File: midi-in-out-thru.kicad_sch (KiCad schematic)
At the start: 24 parts, among them J1 uC, J2 IN, J3 OUT, J4 THRU, U1 74HC14, U2 H11L1

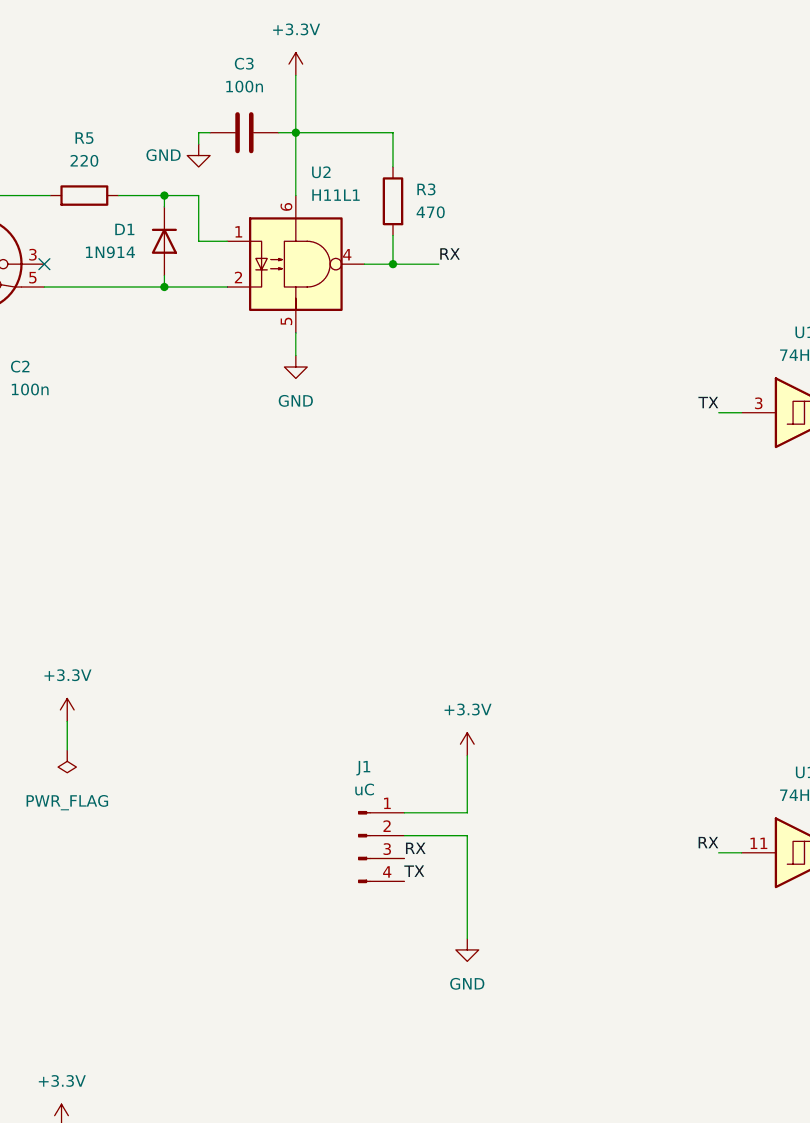
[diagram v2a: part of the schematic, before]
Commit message: Smaller resistors, neater layout
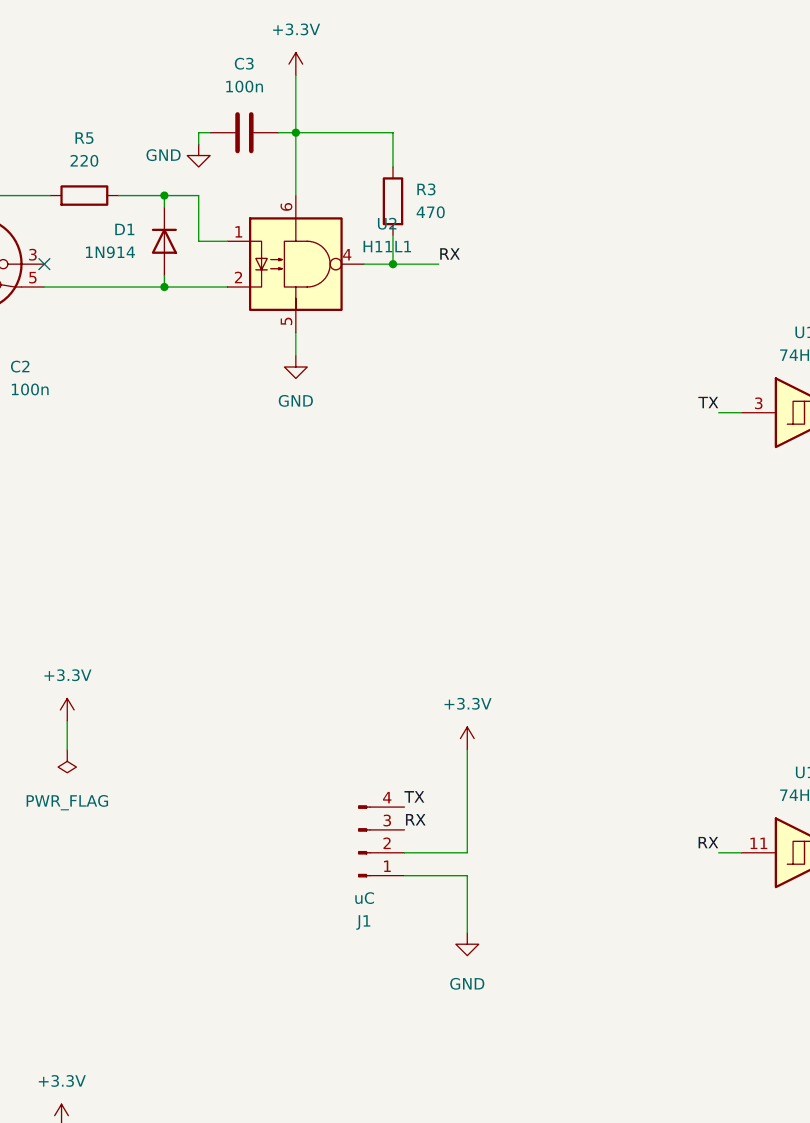
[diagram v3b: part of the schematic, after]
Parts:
- H1, H2, H3, H4: footprint MountingHole:MountingHole_3.2mm_M3 -> Personal:MountingHole_3.2mm_M3
- R1, R2, R3, R5, R6, R7, R8, R9: footprint Resistor_THT:R_Axial_DIN0207_L6.3mm_D2.5mm_P10.16mm_Horizontal -> Resistor_THT:R_Axial_DIN0204_L3.6mm_D1.6mm_P7.62mm_Horizontal
- U1: footprint Package_DIP:DIP-14_W7.62mm_Socket -> Package_DIP:DIP-14_W7.62mm
- U2: footprint Package_DIP:DIP-6_W7.62mm_Socket -> Package_DIP:DIP-6_W7.62mm
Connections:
- net +3.3V: now also J1.2 (Pin_2); no longer J1.1 (Pin_1)
- net GND: now also J1.1 (Pin_1); no longer J1.2 (Pin_2)
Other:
- moved on the sheet: J1
